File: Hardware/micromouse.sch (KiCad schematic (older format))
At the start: 24 parts, among them U1 STM32H743VITx, Y1 NX3225GD-8.000M-EXS00A-CG04874

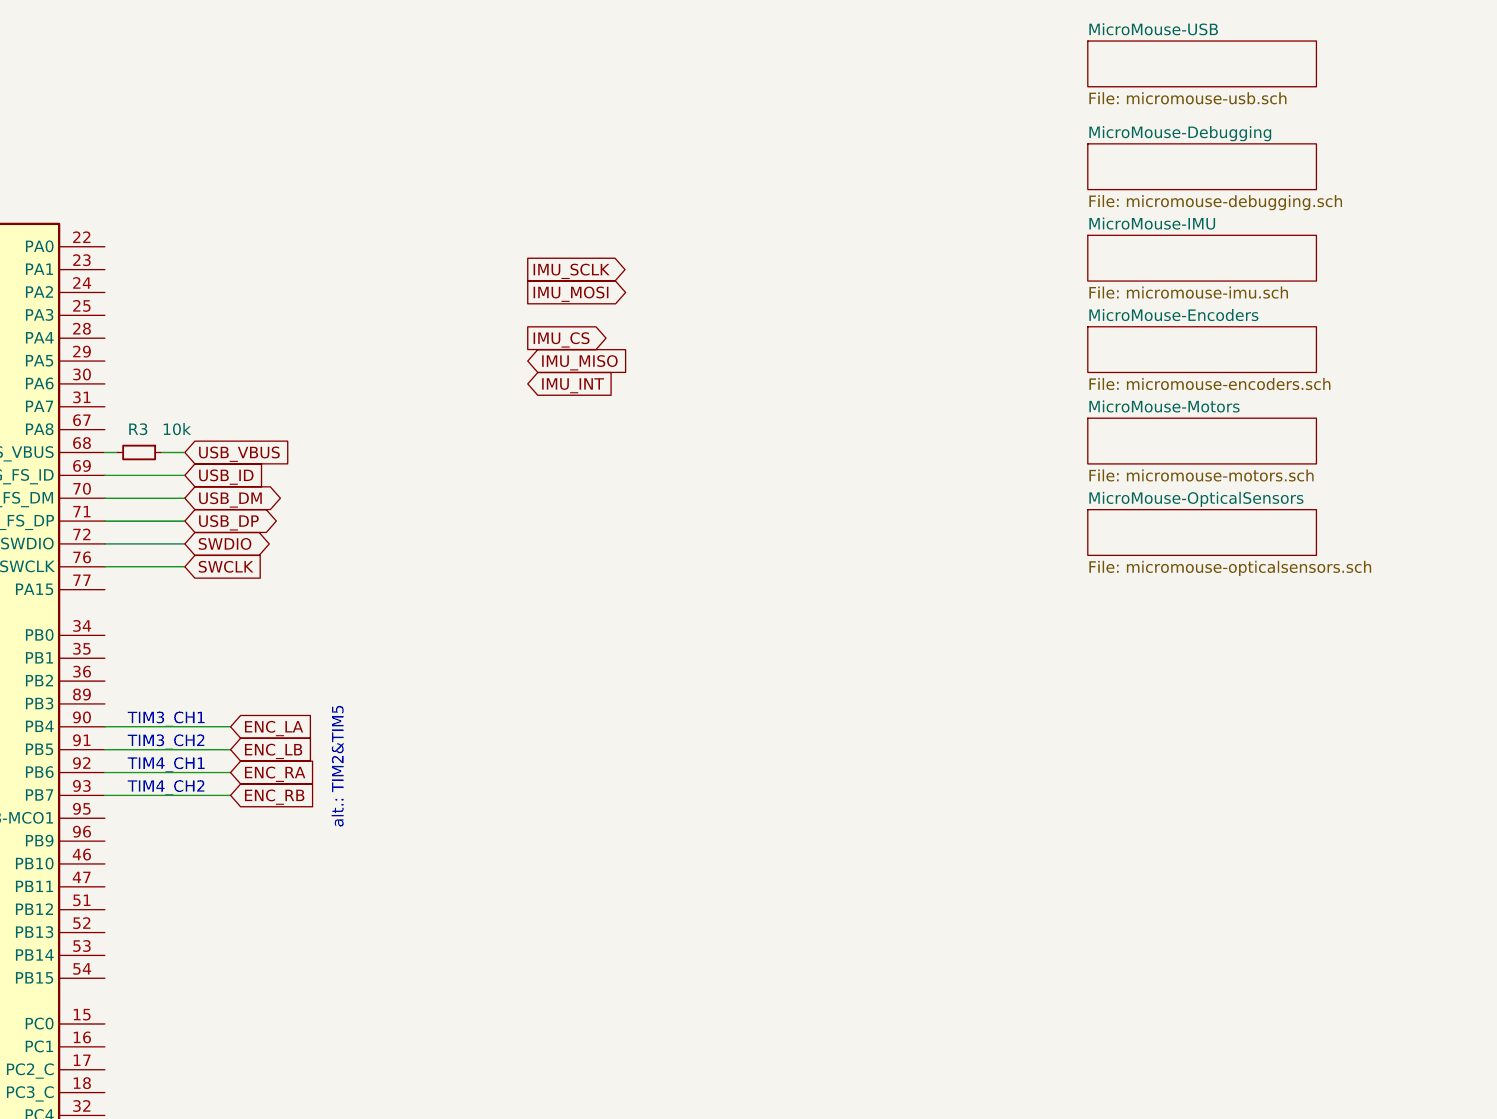
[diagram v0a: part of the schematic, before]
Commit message: add power sub-schematic, fix some supply-connections, rearrange sub-schematics
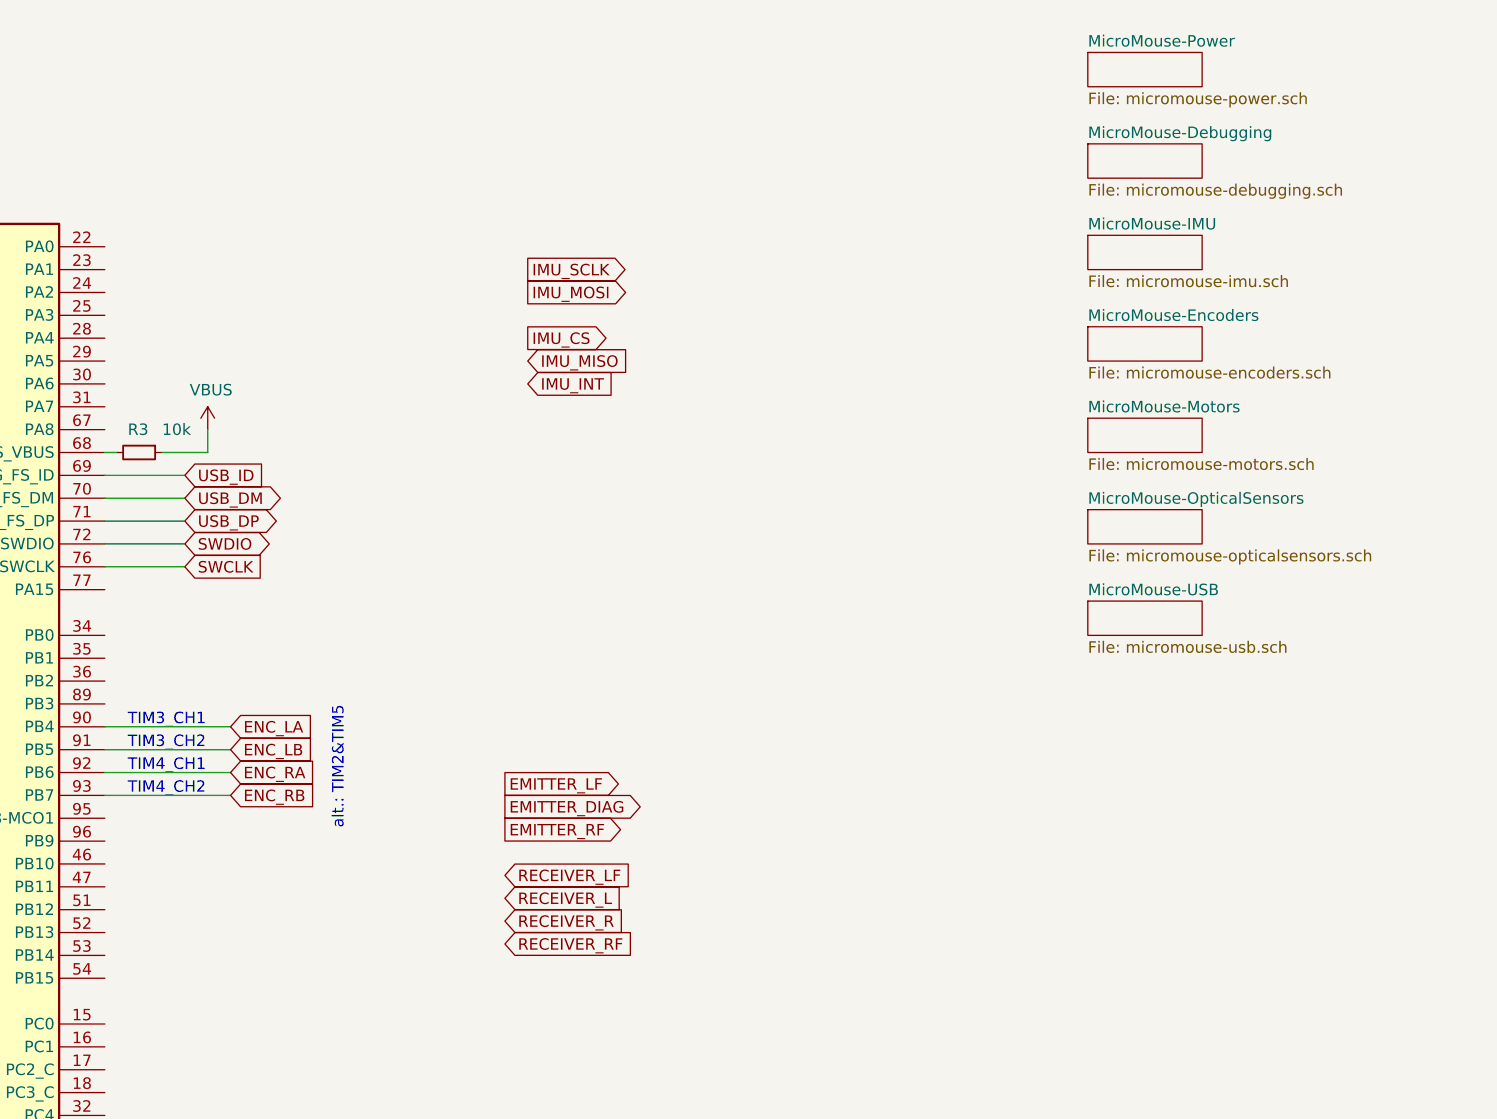
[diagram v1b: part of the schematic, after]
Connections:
- net USB_VBUS renamed VBUS
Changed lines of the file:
@@
 $Descr A4 11693 8268
 encoding utf-8
-Sheet 1 7
+Sheet 1 8
 Title ""
 Date ""
@@
 Wire Wire Line
 	5450 2550 5500 2550
-Text GLabel 5800 2550 2    50   Input ~ 0
-USB_VBUS
 Text GLabel 5800 2650 2    50   Input ~ 0
 USB_ID
@@
 	5450 2650 5800 2650
 Wire Wire Line
-	5800 2550 5700 2550
+	5900 2550 5700 2550
 $Comp
 L power:VDDA #PWR014
@@
 	3500 1450 3500 1650
 $Sheet
-S 9750 750  1000 200
+S 9750 3200 500  150
 U 5C924FF5
 F0 "MicroMouse-USB" 50
@@
 $EndSheet
 $Sheet
-S 9750 1200 1000 200
+S 9750 1200 500  150
 U 5C92AF24
 F0 "MicroMouse-Debugging" 50
@@
 $EndSheet
 $Sheet
-S 9750 1600 1000 200
+S 9750 1600 500  150
 U 5CAF83BA
 F0 "MicroMouse-IMU" 50
@@
 ENC_LB
 $Sheet
-S 9750 2000 1000 200
+S 9750 2000 500  150
 U 5CBCE166
 F0 "MicroMouse-Encoders" 50
@@
 	5450 3750 6000 3750
 $Sheet
-S 9750 2400 1000 200
+S 9750 2400 500  150
 U 5CBF5B75
 F0 "MicroMouse-Motors" 50
@@
 	3650 4450 3000 4450
 $Sheet
-S 9750 2800 1000 200
+S 9750 2800 500  150
 U 5C8AD6BB
 F0 "MicroMouse-OpticalSensors" 50
@@
 	1    0    0    -1
 $EndComp
+Text GLabel 7200 4400 2    50   Input ~ 0
+RECEIVER_LF
+Text GLabel 7200 4500 2    50   Input ~ 0
+RECEIVER_L
+Text GLabel 7200 4600 2    50   Input ~ 0
+RECEIVER_R
+Text GLabel 7200 4700 2    50   Input ~ 0
+RECEIVER_RF
+Text GLabel 7200 4000 2    50   Output ~ 0
+EMITTER_LF
+Text GLabel 7200 4100 2    50   Output ~ 0
+EMITTER_DIAG
+Text GLabel 7200 4200 2    50   Output ~ 0
+EMITTER_RF
+$Sheet
+S 9750 800  500  150
+U 5C8B0761
+F0 "MicroMouse-Power" 50
+F1 "micromouse-power.sch" 50
+$EndSheet
+$Comp
+L power:VBUS #PWR?
+U 1 1 5C8B6706
+P 5900 2450
+F 0 "#PWR?" H 5900 2300 50  0001 C CNN
+F 1 "VBUS" H 5915 2623 50  0000 C CNN
+F 2 "" H 5900 2450 50  0001 C CNN
+F 3 "" H 5900 2450 50  0001 C CNN
+	1    5900 2450
+	1    0    0    -1
+$EndComp
+Wire Wire Line
+	5900 2550 5900 2450
 $EndSCHEMATC

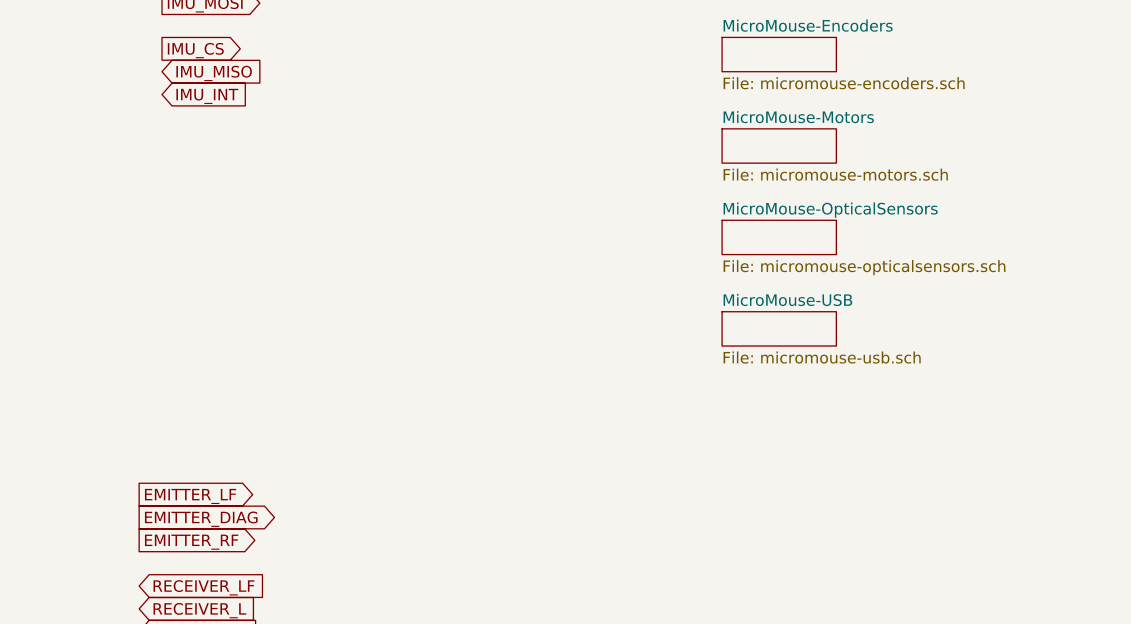
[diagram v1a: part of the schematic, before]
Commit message: [OLED]  - added kicad display lib for ssd1306 oled display footorint  - added ssd1306 schematic part  - added display plus signals into micromouse schematics
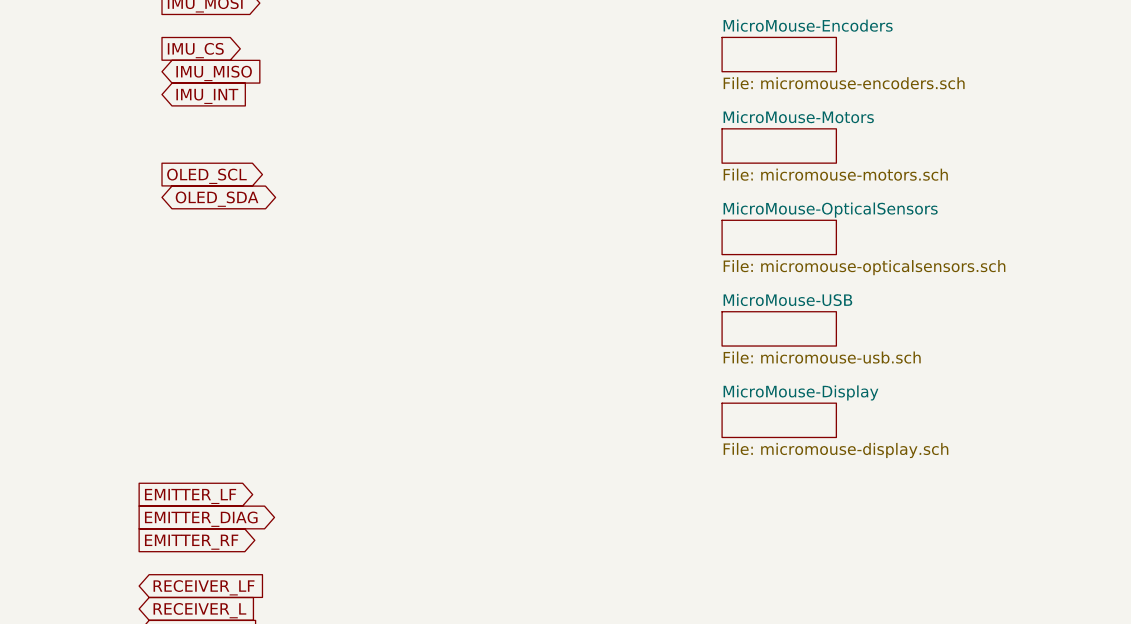
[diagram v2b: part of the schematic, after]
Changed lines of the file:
@@
 $Descr A4 11693 8268
 encoding utf-8
-Sheet 1 8
+Sheet 1 9
 Title ""
 Date ""
@@
 Wire Wire Line
 	5900 2550 5900 2450
+$Sheet
+S 9750 3600 500  150
+U 5C9073AE
+F0 "MicroMouse-Display" 50
+F1 "micromouse-display.sch" 50
+$EndSheet
+Text GLabel 7300 2600 2    50   Output ~ 0
+OLED_SCL
+Text GLabel 7300 2700 2    50   BiDi ~ 0
+OLED_SDA
 $EndSCHEMATC
